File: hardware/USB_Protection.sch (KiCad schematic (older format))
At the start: 7 parts, among them Q1 DMN6140L, U12 TCPP01-M12

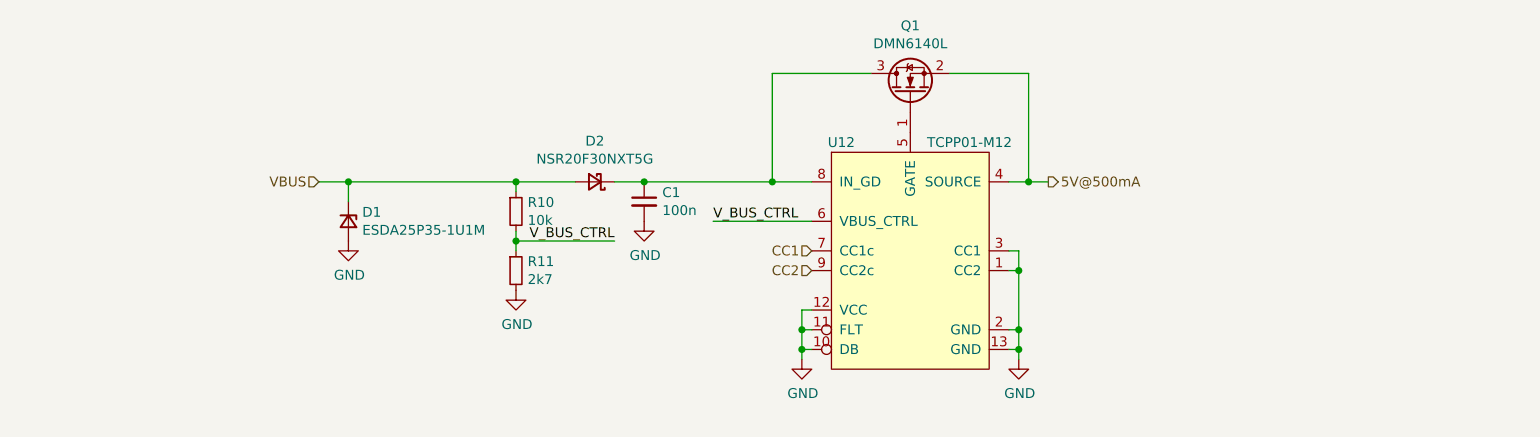
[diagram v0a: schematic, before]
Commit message: fixed usb type c cc pin termination
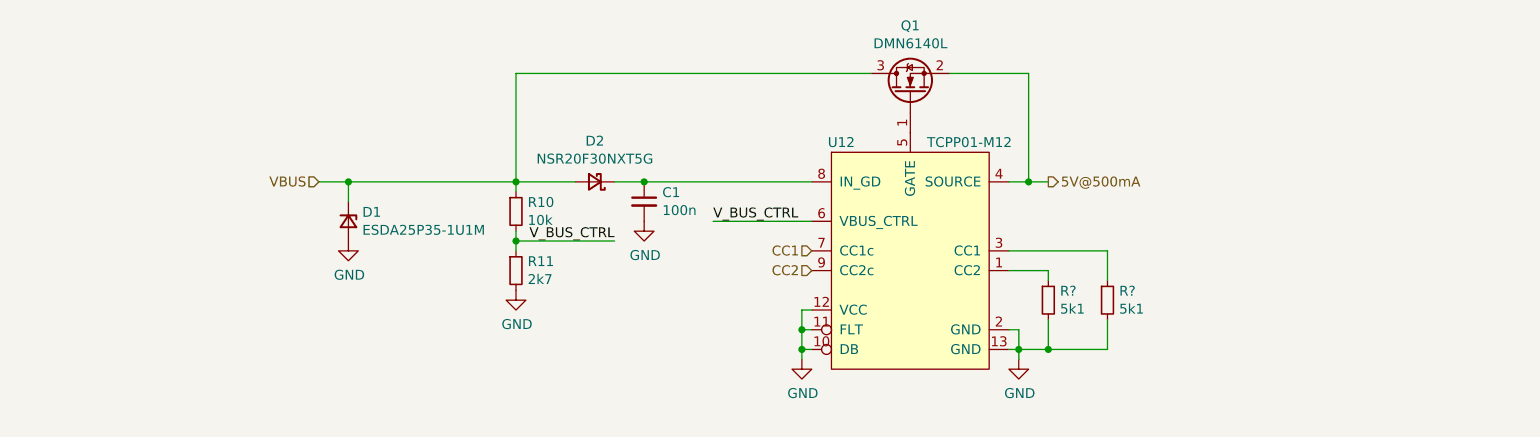
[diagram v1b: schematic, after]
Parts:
- added R? (x2): 5k1, Resistor_SMD:R_0603_1608Metric_Pad1.05x0.95mm_HandSolder, symbol Device:R_Small
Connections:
- net GND: now also R?.2, R?.2; no longer U12.1 (CC2), U12.3 (CC1)
- net VBUS: now also Q1.3 (D)
- net at C1.1, D2.1 (K), U12.8 (IN_GD): no longer Q1.3 (D)
- new net: R?.1, U12.1 (CC2)
- new net: R?.1, U12.3 (CC1)
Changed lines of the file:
@@
 $EndComp
-Wire Wire Line
-	5550 3100 5500 3100
-Wire Wire Line
-	5550 3100 5550 3200
 Wire Wire Line
 	5500 3500 5550 3500
-Connection ~ 5550 3500
 Wire Wire Line
 	5550 3500 5550 3600
@@
 Wire Wire Line
 	4000 2950 4500 2950
-Wire Wire Line
-	3650 2750 4300 2750
-Wire Wire Line
-	5500 3200 5550 3200
-Connection ~ 5550 3200
-Wire Wire Line
-	5550 3200 5550 3500
 $Comp
 L Transistor_FET:DMN6140L Q1
@@
 $EndComp
 Wire Wire Line
-	4800 2200 4300 2200
-Wire Wire Line
-	4300 2200 4300 2750
-Connection ~ 4300 2750
-Wire Wire Line
-	4300 2750 4500 2750
-Wire Wire Line
 	5200 2200 5600 2200
 Wire Wire Line
@@
 	5700 2750 5600 2750
 Connection ~ 5600 2750
+Wire Wire Line
+	3650 2750 4500 2750
+Wire Wire Line
+	3000 2200 3000 2750
+Wire Wire Line
+	3000 2200 4800 2200
+$Comp
+L Device:R_Small R?
+U 1 1 605C8234
+P 5700 3350
+F 0 "R?" H 5759 3396 50  0000 L CNN
+F 1 "5k1" H 5759 3305 50  0000 L CNN
+F 2 "Resistor_SMD:R_0603_1608Metric_Pad1.05x0.95mm_HandSolder" H 5700 3350 50  0001 C CNN
+F 3 "~" H 5700 3350 50  0001 C CNN
+	1    5700 3350
+	1    0    0    -1
+$EndComp
+$Comp
+L Device:R_Small R?
+U 1 1 605C8525
+P 6000 3350
+F 0 "R?" H 6059 3396 50  0000 L CNN
+F 1 "5k1" H 6059 3305 50  0000 L CNN
+F 2 "Resistor_SMD:R_0603_1608Metric_Pad1.05x0.95mm_HandSolder" H 6000 3350 50  0001 C CNN
+F 3 "~" H 6000 3350 50  0001 C CNN
+	1    6000 3350
+	1    0    0    -1
+$EndComp
+Wire Wire Line
+	5700 3200 5700 3250
+Wire Wire Line
+	5500 3200 5700 3200
+Wire Wire Line
+	6000 3100 6000 3250
+Wire Wire Line
+	5500 3100 6000 3100
+Wire Wire Line
+	5700 3450 5700 3600
+Wire Wire Line
+	5700 3600 5550 3600
+Wire Wire Line
+	6000 3450 6000 3600
+Wire Wire Line
+	6000 3600 5700 3600
+Connection ~ 5700 3600
 $EndSCHEMATC

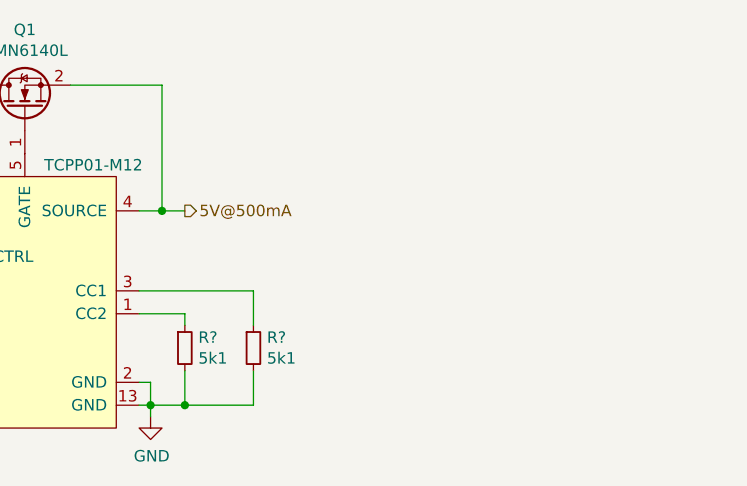
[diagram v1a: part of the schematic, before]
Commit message: reverse current protection
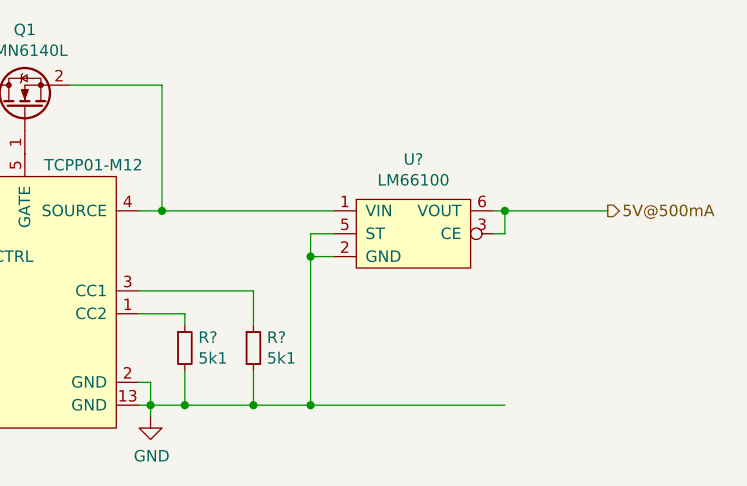
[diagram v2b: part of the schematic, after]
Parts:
- added U?: LM66100, lm66100:LM66100DCKT, symbol watch:LM66100-Variant2
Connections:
- net 5V@500mA: now also U?.3 (CE), U?.6 (VOUT); no longer Q1.2 (S), U12.4 (SOURCE)
- net GND: now also U?.2 (GND), U?.5 (ST)
- new net: Q1.2 (S), U12.4 (SOURCE), U?.1 (VIN)
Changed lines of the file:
@@
 Wire Wire Line
 	5600 2750 5500 2750
-Text HLabel 5700 2750 2    50   Output ~ 0
+Text HLabel 7550 2750 2    50   Output ~ 0
 5V@500mA
-Wire Wire Line
-	5700 2750 5600 2750
 Connection ~ 5600 2750
 Wire Wire Line
@@
 	6000 3600 5700 3600
 Connection ~ 5700 3600
+Wire Wire Line
+	5600 2750 6350 2750
+Wire Wire Line
+	6350 2950 6250 2950
+Wire Wire Line
+	6250 2950 6250 3600
+Wire Wire Line
+	6250 3600 6000 3600
+Connection ~ 6000 3600
+Wire Wire Line
+	7100 3600 6250 3600
+Connection ~ 6250 3600
+$Comp
+L watch:LM66100-Variant2 U?
+U 1 1 605D85BE
+P 6700 2850
+F 0 "U?" H 6700 3175 50  0000 C CNN
+F 1 "LM66100" H 6700 3084 50  0000 C CNN
+F 2 "lm66100:LM66100DCKT" H 7050 3100 50  0001 C CNN
+F 3 "" H 7050 3100 50  0001 C CNN
+	1    6700 2850
+	1    0    0    -1
+$EndComp
+Wire Wire Line
+	7050 2750 7100 2750
+Wire Wire Line
+	6350 2850 6250 2850
+Wire Wire Line
+	6250 2850 6250 2950
+Connection ~ 6250 2950
+Wire Wire Line
+	7050 2850 7100 2850
+Wire Wire Line
+	7100 2850 7100 2750
+Connection ~ 7100 2750
+Wire Wire Line
+	7100 2750 7550 2750
 $EndSCHEMATC

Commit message: hardware development
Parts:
- removed R? (x2): 5k1, Resistor_SMD:R_0603_1608Metric_Pad1.05x0.95mm_HandSolder, symbol Device:R_Small
- removed U?: LM66100, lm66100:LM66100DCKT, symbol watch:LM66100-Variant2
- added D?: SMBJ5.0CA-Q, Diode_SMD:D_0603_1608Metric_Pad1.05x0.95mm_HandSolder, symbol Device:D_Zener_Small
- added F?: 1812L050/60MR, symbol Device:Polyfuse_Small
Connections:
- wire segments 45 -> 37
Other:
- note added: "Don't need Rd, handled inside the chip"
- moved on the sheet: D1, D2, R10, R11
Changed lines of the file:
@@
 $Descr A4 11693 8268
 encoding utf-8
-Sheet 2 3
+Sheet 3 4
 Title ""
 Date ""
@@
 AR Path="/6072C21E" Ref="U?"  Part="1"
 AR Path="/6071FFAF/6072C21E" Ref="U12"  Part="1"
+AR Path="/60604F0C/6060934C/6072C21E" Ref="U?"  Part="1"
 F 0 "U12" H 4650 3750 50  0000 C CNN
 F 1 "TCPP01-M12" H 5300 3750 50  0000 C CNN
@@
 L Device:D_Zener_Small D?
 U 1 1 60731C37
-P 2150 2950
+P 2100 2400
 AR Path="/60731C37" Ref="D?"  Part="1"
 AR Path="/6071FFAF/60731C37" Ref="D1"  Part="1"
-F 0 "D1" V 2104 3020 50  0000 L CNN
-F 1 "ESDA25P35-1U1M" V 2195 3020 50  0000 L CNN
-F 2 "Diode_SMD:D_0603_1608Metric_Pad1.05x0.95mm_HandSolder" V 2150 2950 50  0001 C CNN
-F 3 "~" V 2150 2950 50  0001 C CNN
-	1    2150 2950
+AR Path="/60604F0C/6060934C/60731C37" Ref="D?"  Part="1"
+F 0 "D1" V 2054 2470 50  0000 L CNN
+F 1 "ESDA25P35-1U1M" V 2145 2470 50  0000 L CNN
+F 2 "Diode_SMD:D_0603_1608Metric_Pad1.05x0.95mm_HandSolder" V 2100 2400 50  0001 C CNN
+F 3 "~" V 2100 2400 50  0001 C CNN
+	1    2100 2400
 	0    1    1    0
 $EndComp
-Text HLabel 2000 2750 0    50   Input ~ 0
+Text HLabel 1650 2200 0    50   Input ~ 0
 VBUS
 Text HLabel 4500 3100 0    50   Input ~ 0
@@
 U 1 1 605BE08D
 P 5550 3650
+AR Path="/6071FFAF/605BE08D" Ref="#PWR0130"  Part="1"
+AR Path="/60604F0C/6060934C/605BE08D" Ref="#PWR?"  Part="1"
 F 0 "#PWR0130" H 5550 3400 50  0001 C CNN
 F 1 "GND" H 5555 3477 50  0000 C CNN
@@
 U 1 1 605BEA49
 P 4450 3650
+AR Path="/6071FFAF/605BEA49" Ref="#PWR0131"  Part="1"
+AR Path="/60604F0C/6060934C/605BEA49" Ref="#PWR?"  Part="1"
 F 0 "#PWR0131" H 4450 3400 50  0001 C CNN
 F 1 "GND" H 4455 3477 50  0000 C CNN
@@
 	4450 3600 4450 3500
 Wire Wire Line
-	2150 2850 2150 2750
-Wire Wire Line
-	2150 2750 2000 2750
+	2100 2300 2100 2200
 $Comp
 L Device:R_Small R10
 U 1 1 605BF926
-P 3000 2900
-F 0 "R10" H 3059 2946 50  0000 L CNN
-F 1 "10k" H 3059 2855 50  0000 L CNN
-F 2 "Resistor_SMD:R_0603_1608Metric_Pad1.05x0.95mm_HandSolder" H 3000 2900 50  0001 C CNN
-F 3 "~" H 3000 2900 50  0001 C CNN
-	1    3000 2900
+P 3000 2400
+AR Path="/6071FFAF/605BF926" Ref="R10"  Part="1"
+AR Path="/60604F0C/6060934C/605BF926" Ref="R?"  Part="1"
+F 0 "R10" H 3059 2446 50  0000 L CNN
+F 1 "10k" H 3059 2355 50  0000 L CNN
+F 2 "Resistor_SMD:R_0603_1608Metric_Pad1.05x0.95mm_HandSolder" H 3000 2400 50  0001 C CNN
+F 3 "~" H 3000 2400 50  0001 C CNN
+	1    3000 2400
 	1    0    0    -1
 $EndComp
@@
 L Device:R_Small R11
 U 1 1 605C0410
-P 3000 3200
-F 0 "R11" H 3059 3246 50  0000 L CNN
-F 1 "2k7" H 3059 3155 50  0000 L CNN
-F 2 "Resistor_SMD:R_0603_1608Metric_Pad1.05x0.95mm_HandSolder" H 3000 3200 50  0001 C CNN
-F 3 "~" H 3000 3200 50  0001 C CNN
-	1    3000 3200
-	1    0    0    -1
-$EndComp
-Wire Wire Line
-	2150 2750 3000 2750
-Wire Wire Line
-	3000 2750 3000 2800
-Connection ~ 2150 2750
+P 3000 2700
+AR Path="/6071FFAF/605C0410" Ref="R11"  Part="1"
+AR Path="/60604F0C/6060934C/605C0410" Ref="R?"  Part="1"
+F 0 "R11" H 3059 2746 50  0000 L CNN
+F 1 "2k7" H 3059 2655 50  0000 L CNN
+F 2 "Resistor_SMD:R_0603_1608Metric_Pad1.05x0.95mm_HandSolder" H 3000 2700 50  0001 C CNN
+F 3 "~" H 3000 2700 50  0001 C CNN
+	1    3000 2700
+	1    0    0    -1
+$EndComp
 $Comp
 L Device:D_Schottky_Small D2
 U 1 1 605C65BD
-P 3400 2750
-F 0 "D2" H 3400 2543 50  0000 C CNN
-F 1 "NSR20F30NXT5G" H 3400 2634 50  0000 C CNN
-F 2 "Diode_SMD:D_0603_1608Metric_Pad1.05x0.95mm_HandSolder" V 3400 2750 50  0001 C CNN
-F 3 "~" V 3400 2750 50  0001 C CNN
-	1    3400 2750
-	-1   0    0    1
+P 3650 2500
+AR Path="/6071FFAF/605C65BD" Ref="D2"  Part="1"
+AR Path="/60604F0C/6060934C/605C65BD" Ref="D?"  Part="1"
+F 0 "D2" V 3750 2400 50  0000 C CNN
+F 1 "NSR20F30NXT5G" V 3550 2150 50  0000 C CNN
+F 2 "Diode_SMD:D_0603_1608Metric_Pad1.05x0.95mm_HandSolder" V 3650 2500 50  0001 C CNN
+F 3 "~" V 3650 2500 50  0001 C CNN
+	1    3650 2500
+	0    -1   -1   0
 $EndComp
 $Comp
@@
 U 1 1 605C70FD
 P 3650 2850
+AR Path="/6071FFAF/605C70FD" Ref="C1"  Part="1"
+AR Path="/60604F0C/6060934C/605C70FD" Ref="C?"  Part="1"
 F 0 "C1" H 3742 2896 50  0000 L CNN
 F 1 "100n" H 3742 2805 50  0000 L CNN
@@
 L power:GND #PWR0132
 U 1 1 605BDB68
-P 2150 3050
-F 0 "#PWR0132" H 2150 2800 50  0001 C CNN
-F 1 "GND" H 2155 2877 50  0000 C CNN
-F 2 "" H 2150 3050 50  0001 C CNN
-F 3 "" H 2150 3050 50  0001 C CNN
-	1    2150 3050
+P 2100 2500
+AR Path="/6071FFAF/605BDB68" Ref="#PWR0132"  Part="1"
+AR Path="/60604F0C/6060934C/605BDB68" Ref="#PWR?"  Part="1"
+F 0 "#PWR0132" H 2100 2250 50  0001 C CNN
+F 1 "GND" H 2105 2327 50  0000 C CNN
+F 2 "" H 2100 2500 50  0001 C CNN
+F 3 "" H 2100 2500 50  0001 C CNN
+	1    2100 2500
 	1    0    0    -1
 $EndComp
@@
 L power:GND #PWR0133
 U 1 1 605C1A8E
-P 3000 3300
-F 0 "#PWR0133" H 3000 3050 50  0001 C CNN
-F 1 "GND" H 3005 3127 50  0000 C CNN
-F 2 "" H 3000 3300 50  0001 C CNN
-F 3 "" H 3000 3300 50  0001 C CNN
-	1    3000 3300
-	1    0    0    -1
-$EndComp
-Wire Wire Line
-	3000 3000 3000 3050
-Wire Wire Line
-	3300 2750 3000 2750
-Connection ~ 3000 2750
+P 3000 2800
+AR Path="/6071FFAF/605C1A8E" Ref="#PWR0133"  Part="1"
+AR Path="/60604F0C/6060934C/605C1A8E" Ref="#PWR?"  Part="1"
+F 0 "#PWR0133" H 3000 2550 50  0001 C CNN
+F 1 "GND" H 3005 2627 50  0000 C CNN
+F 2 "" H 3000 2800 50  0001 C CNN
+F 3 "" H 3000 2800 50  0001 C CNN
+	1    3000 2800
+	1    0    0    -1
+$EndComp
+Wire Wire Line
+	3000 2500 3000 2550
 $Comp
 L power:GND #PWR0136
 U 1 1 605CCB83
 P 3650 2950
+AR Path="/6071FFAF/605CCB83" Ref="#PWR0136"  Part="1"
+AR Path="/60604F0C/6060934C/605CCB83" Ref="#PWR?"  Part="1"
 F 0 "#PWR0136" H 3650 2700 50  0001 C CNN
 F 1 "GND" H 3655 2777 50  0000 C CNN
@@
 	1    0    0    -1
 $EndComp
-Wire Wire Line
-	3500 2750 3650 2750
-Connection ~ 3650 2750
-Text Label 3500 3050 2    50   ~ 0
+Text Label 3500 2550 2    50   ~ 0
 V_BUS_CTRL
 Wire Wire Line
-	3500 3050 3000 3050
-Connection ~ 3000 3050
-Wire Wire Line
-	3000 3050 3000 3100
+	3500 2550 3000 2550
+Connection ~ 3000 2550
+Wire Wire Line
+	3000 2550 3000 2600
 Text Label 4000 2950 0    50   ~ 0
 V_BUS_CTRL
@@
 U 1 1 605D3F9F
 P 5000 2300
+AR Path="/6071FFAF/605D3F9F" Ref="Q1"  Part="1"
+AR Path="/60604F0C/6060934C/605D3F9F" Ref="Q?"  Part="1"
 F 0 "Q1" V 5342 2300 50  0000 C CNN
 F 1 "DMN6140L" V 5251 2300 50  0000 C CNN
@@
 Wire Wire Line
 	5600 2750 5500 2750
-Text HLabel 7550 2750 2    50   Output ~ 0
+Text HLabel 5900 2750 2    50   Output ~ 0
 5V@500mA
 Connection ~ 5600 2750
@@
 	3650 2750 4500 2750
 Wire Wire Line
-	3000 2200 3000 2750
-Wire Wire Line
-	3000 2200 4800 2200
-$Comp
-L Device:R_Small R?
-U 1 1 605C8234
-P 5700 3350
-F 0 "R?" H 5759 3396 50  0000 L CNN
-F 1 "5k1" H 5759 3305 50  0000 L CNN
-F 2 "Resistor_SMD:R_0603_1608Metric_Pad1.05x0.95mm_HandSolder" H 5700 3350 50  0001 C CNN
-F 3 "~" H 5700 3350 50  0001 C CNN
-	1    5700 3350
-	1    0    0    -1
-$EndComp
-$Comp
-L Device:R_Small R?
-U 1 1 605C8525
-P 6000 3350
-F 0 "R?" H 6059 3396 50  0000 L CNN
-F 1 "5k1" H 6059 3305 50  0000 L CNN
-F 2 "Resistor_SMD:R_0603_1608Metric_Pad1.05x0.95mm_HandSolder" H 6000 3350 50  0001 C CNN
-F 3 "~" H 6000 3350 50  0001 C CNN
-	1    6000 3350
-	1    0    0    -1
-$EndComp
-Wire Wire Line
-	5700 3200 5700 3250
-Wire Wire Line
-	5500 3200 5700 3200
-Wire Wire Line
-	6000 3100 6000 3250
-Wire Wire Line
-	5500 3100 6000 3100
-Wire Wire Line
-	5700 3450 5700 3600
-Wire Wire Line
-	5700 3600 5550 3600
-Wire Wire Line
-	6000 3450 6000 3600
-Wire Wire Line
-	6000 3600 5700 3600
-Connection ~ 5700 3600
-Wire Wire Line
-	5600 2750 6350 2750
-Wire Wire Line
-	6350 2950 6250 2950
-Wire Wire Line
-	6250 2950 6250 3600
-Wire Wire Line
-	6250 3600 6000 3600
-Connection ~ 6000 3600
-Wire Wire Line
-	7100 3600 6250 3600
-Connection ~ 6250 3600
-$Comp
-L watch:LM66100-Variant2 U?
-U 1 1 605D85BE
-P 6700 2850
-F 0 "U?" H 6700 3175 50  0000 C CNN
-F 1 "LM66100" H 6700 3084 50  0000 C CNN
-F 2 "lm66100:LM66100DCKT" H 7050 3100 50  0001 C CNN
-F 3 "" H 7050 3100 50  0001 C CNN
-	1    6700 2850
-	1    0    0    -1
-$EndComp
-Wire Wire Line
-	7050 2750 7100 2750
-Wire Wire Line
-	6350 2850 6250 2850
-Wire Wire Line
-	6250 2850 6250 2950
-Connection ~ 6250 2950
-Wire Wire Line
-	7050 2850 7100 2850
-Wire Wire Line
-	7100 2850 7100 2750
-Connection ~ 7100 2750
-Wire Wire Line
-	7100 2750 7550 2750
+	3000 2200 3650 2200
+Wire Wire Line
+	5600 2750 5850 2750
+Wire Wire Line
+	5550 3600 5850 3600
+Wire Wire Line
+	5550 3500 5550 3200
+Wire Wire Line
+	5550 3100 5500 3100
+Connection ~ 5550 3500
+Wire Wire Line
+	5500 3200 5550 3200
+Connection ~ 5550 3200
+Wire Wire Line
+	5550 3200 5550 3100
+$Comp
+L Device:D_Zener_Small D?
+U 1 1 605F2ABA
+P 5850 3100
+AR Path="/605F2ABA" Ref="D?"  Part="1"
+AR Path="/6071FFAF/605F2ABA" Ref="D?"  Part="1"
+AR Path="/60604F0C/6060934C/605F2ABA" Ref="D?"  Part="1"
+F 0 "D?" V 5804 3170 50  0000 L CNN
+F 1 "SMBJ5.0CA-Q" V 5895 3170 50  0000 L CNN
+F 2 "Diode_SMD:D_0603_1608Metric_Pad1.05x0.95mm_HandSolder" V 5850 3100 50  0001 C CNN
+F 3 "~" V 5850 3100 50  0001 C CNN
+	1    5850 3100
+	0    1    1    0
+$EndComp
+Wire Wire Line
+	5850 2750 5850 3000
+Wire Wire Line
+	5850 3200 5850 3600
+Text Notes 4500 3950 0    50   ~ 0
+Don't need Rd, handled inside the chip
+$Comp
+L Device:Polyfuse_Small F?
+U 1 1 6064BF52
+P 1850 2200
+F 0 "F?" V 2055 2200 50  0000 C CNN
+F 1 "1812L050/60MR" V 1964 2200 50  0000 C CNN
+F 2 "" H 1900 2000 50  0001 L CNN
+F 3 "~" H 1850 2200 50  0001 C CNN
+	1    1850 2200
+	0    -1   -1   0
+$EndComp
+Wire Wire Line
+	1950 2200 2100 2200
+Wire Wire Line
+	1850 2200 1750 2200
+Wire Wire Line
+	3650 2400 3650 2200
+Connection ~ 3650 2200
+Wire Wire Line
+	3650 2200 4800 2200
+Wire Wire Line
+	3650 2600 3650 2750
+Connection ~ 3650 2750
+Connection ~ 1750 2200
+Wire Wire Line
+	1750 2200 1650 2200
+Wire Wire Line
+	3000 2200 3000 2300
+Wire Wire Line
+	3000 2200 2100 2200
+Connection ~ 3000 2200
+Connection ~ 2100 2200
+Wire Wire Line
+	5900 2750 5850 2750
+Connection ~ 5850 2750
 $EndSCHEMATC
